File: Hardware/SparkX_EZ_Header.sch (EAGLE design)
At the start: 29 parts, among them J1 QWIIC_RIGHT_ANGLE

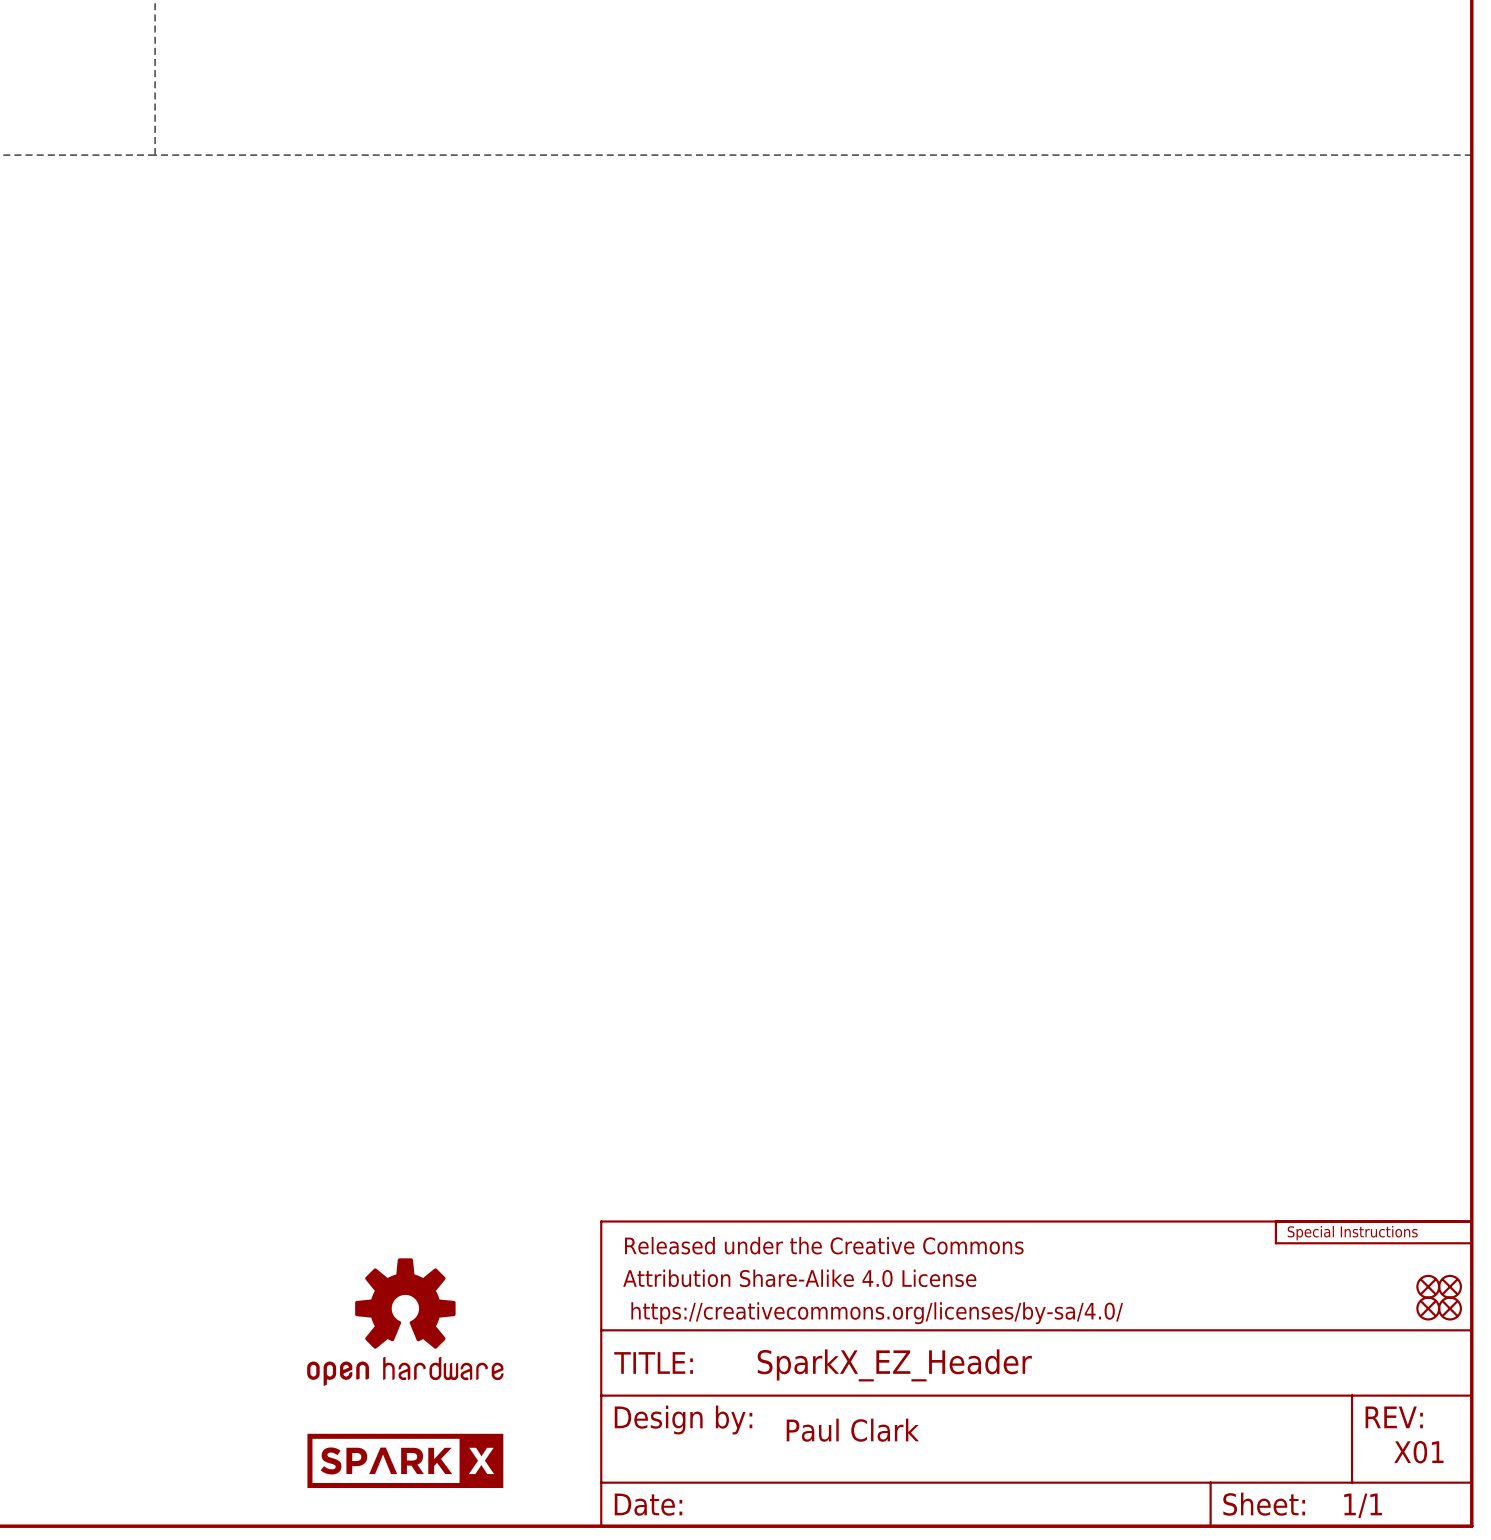
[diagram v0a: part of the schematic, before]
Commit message: Add bottom silk
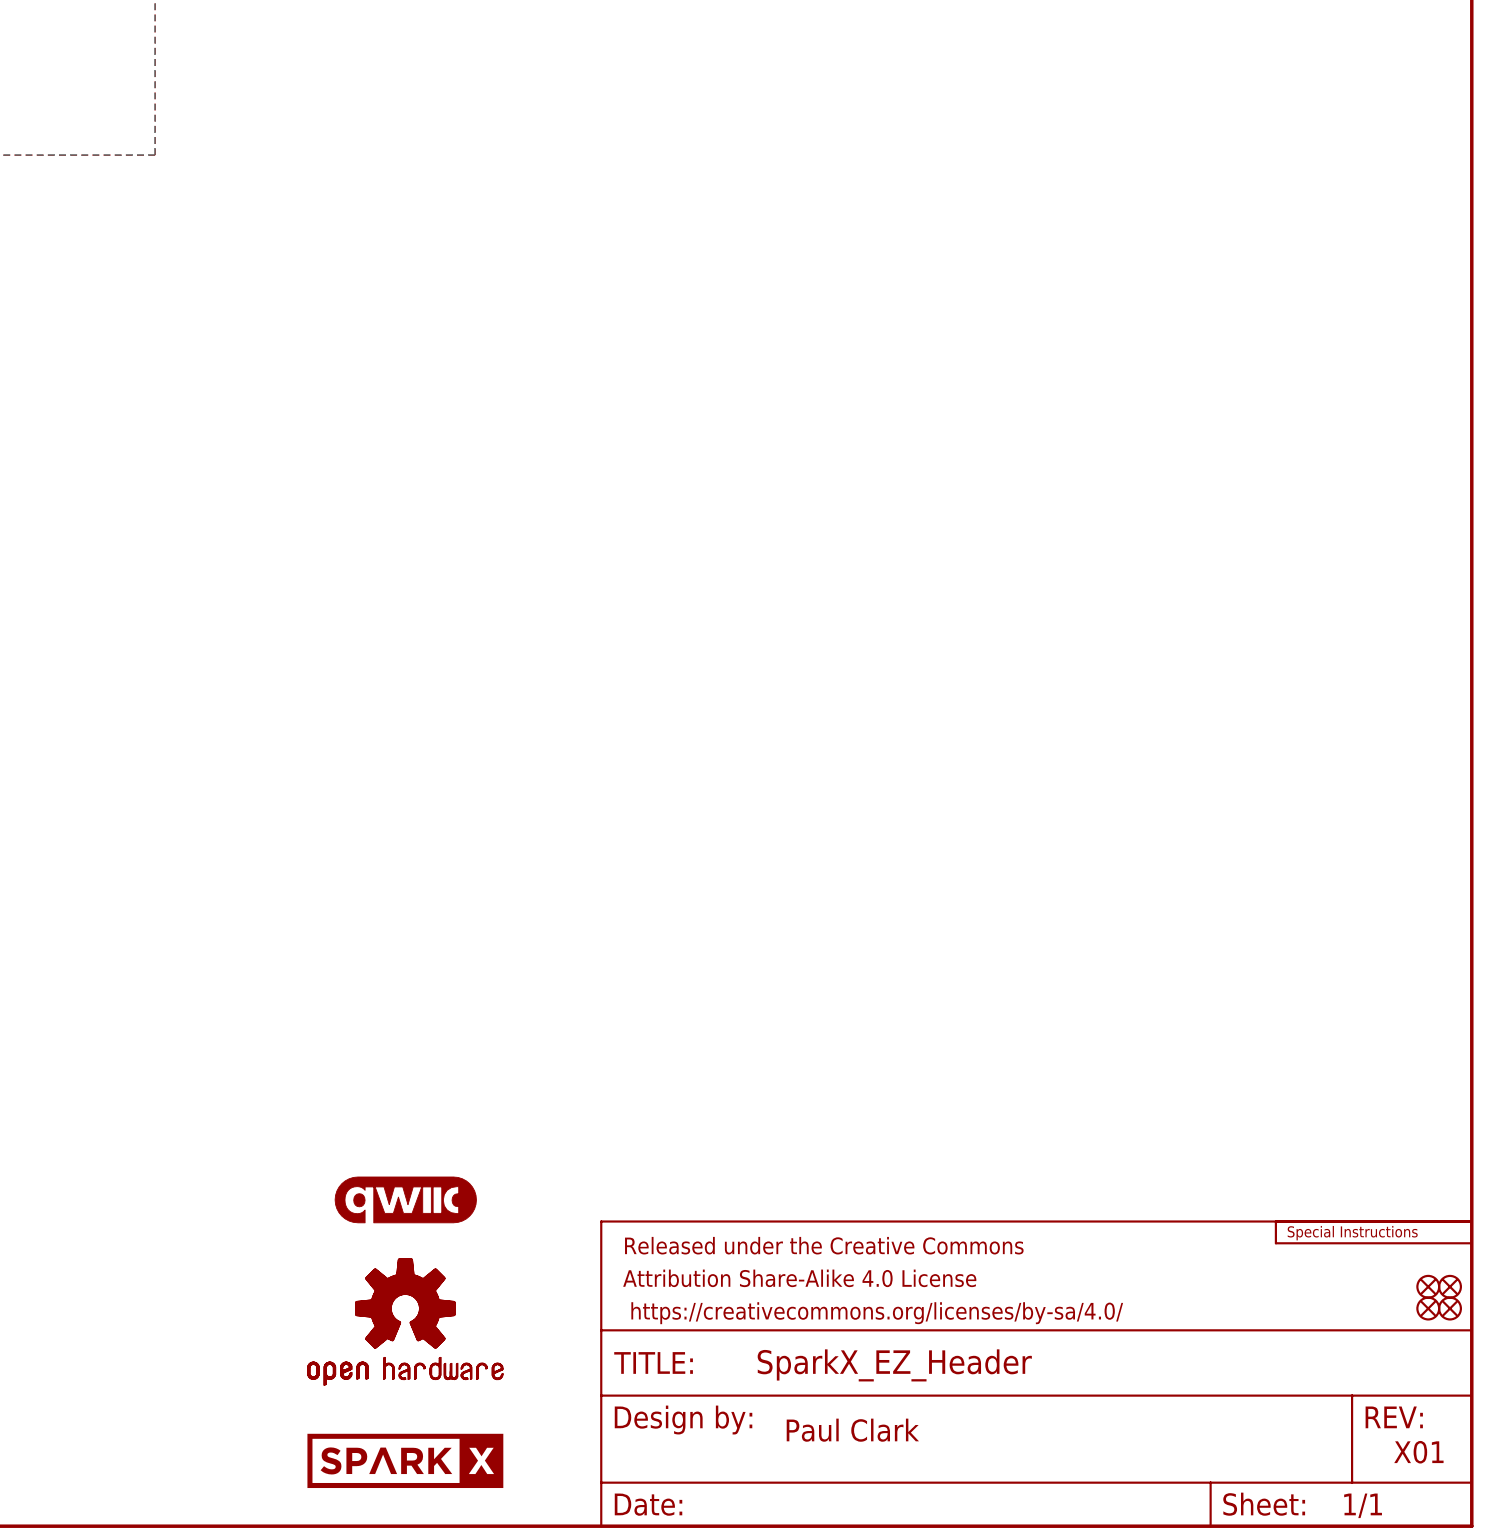
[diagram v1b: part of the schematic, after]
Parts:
- added LOGO3: OSHW-LOGOMINI, SparkFun-Aesthetics:OSHW-LOGOMINI
- added LOGO4: QWIIC_LOGO_5MM, SparkFun-Aesthetics:QWIIC_LOGO_5MM
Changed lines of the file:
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@@
 <part name="I2C" library="SparkFun-Jumpers" deviceset="JUMPER-SMT_3_2-NC_TRACE" device="_SILK" package3d_urn="urn:adsk.eagle:package:39289/1"/>
 <part name="SUPPLY5" library="SparkFun-PowerSymbols" deviceset="3.3V" device=""/>
+<part name="LOGO3" library="SparkFun-Aesthetics" deviceset="OSHW-LOGO" device="MINI"/>
+<part name="LOGO4" library="SparkFun-Aesthetics" deviceset="QWIIC_LOGO" device="_5MM"/>
 </parts>
 <sheets>
@@
 <text x="422.656" y="7.366" size="2.54" layer="94">X01</text>
 <wire x1="88.9" y1="160.02" x2="88.9" y2="279.4" width="0.2032" layer="97" style="longdash"/>
-<wire x1="431.8" y1="160.02" x2="278.13" y2="160.02" width="0.2032" layer="97" style="longdash"/>
 <wire x1="278.13" y1="160.02" x2="88.9" y2="160.02" width="0.2032" layer="97" style="longdash"/>
 <wire x1="201.93" y1="160.02" x2="201.93" y2="279.4" width="0.2032" layer="97" style="longdash"/>
@@
 <attribute name="VALUE" x="238.76" y="204.724" size="1.778" layer="96" align="bottom-center"/>
 </instance>
+<instance part="LOGO3" gate="G$1" x="307.34" y="25.4" smashed="yes"/>
+<instance part="LOGO4" gate="G$1" x="307.34" y="38.1" smashed="yes"/>
 </instances>
 <busses>

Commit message: Update 16-way FPC Connector
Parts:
- OUT: value FPC_16_0.5MM_BACKFLIP -> (none); device New_Parts_Connectors:FPC_16_0.5MM_BACKFLIP -> SparkFun-Connectors:CONN_16FPC_16_0.5MM
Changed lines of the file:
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@@
 <part name="FD3" library="SparkFun-Aesthetics" deviceset="FIDUCIAL" device="UFIDUCIAL" value="FIDUCIALUFIDUCIAL"/>
 <part name="FD4" library="SparkFun-Aesthetics" deviceset="FIDUCIAL" device="UFIDUCIAL" value="FIDUCIALUFIDUCIAL"/>
-<part name="OUT" library="New_Parts_Connectors" deviceset="FPC_16_0.5MM" device="_BACKFLIP"/>
+<part name="OUT" library="SparkFun-Connectors" deviceset="CONN_16" device="FPC_16_0.5MM"/>
 <part name="SUPPLY22" library="SparkFun-PowerSymbols" deviceset="3.3V" device=""/>
 <part name="SUPPLY27" library="SparkFun-PowerSymbols" deviceset="V_USB" device=""/>
@@
 <instance part="FD4" gate="G$1" x="429.26" y="27.94" smashed="yes"/>
 <instance part="LOGO2" gate="G$1" x="307.34" y="25.4" smashed="yes"/>
-<instance part="OUT" gate="G$1" x="53.34" y="215.9" smashed="yes" rot="MR0">
-<attribute name="NAME" x="55.88" y="236.474" size="1.778" layer="95" rot="MR0"/>
-<attribute name="VALUE" x="55.88" y="190.5" size="1.778" layer="96" rot="MR0"/>
+<instance part="OUT" gate="G$1" x="55.88" y="213.36" smashed="yes" rot="R180">
+<attribute name="NAME" x="53.34" y="192.786" size="1.778" layer="95" rot="R180"/>
+<attribute name="VALUE" x="58.42" y="238.76" size="1.778" layer="96" rot="R180"/>
 </instance>
 <instance part="SUPPLY22" gate="G$1" x="43.18" y="236.22" smashed="yes">
 <attribute name="VALUE" x="43.18" y="239.014" size="1.778" layer="96" align="bottom-center"/>
 </instance>
-<instance part="SUPPLY27" gate="G$1" x="35.56" y="195.58" smashed="yes">
-<attribute name="VALUE" x="35.56" y="198.374" size="1.778" layer="96" align="bottom-center"/>
+<instance part="SUPPLY27" gate="G$1" x="27.94" y="198.12" smashed="yes">
+<attribute name="VALUE" x="27.94" y="200.914" size="1.778" layer="96" align="bottom-center"/>
 </instance>
 <instance part="GND56" gate="1" x="40.64" y="187.96" smashed="yes">
@@
 <segment>
 <pinref part="SUPPLY22" gate="G$1" pin="3.3V"/>
-<wire x1="43.18" y1="236.22" x2="43.18" y2="231.14" width="0.1524" layer="91"/>
 <pinref part="OUT" gate="G$1" pin="2"/>
-<wire x1="43.18" y1="231.14" x2="45.72" y2="231.14" width="0.1524" layer="91"/>
 <pinref part="OUT" gate="G$1" pin="15"/>
+<wire x1="45.72" y1="231.14" x2="43.18" y2="231.14" width="0.1524" layer="91"/>
+<wire x1="43.18" y1="231.14" x2="43.18" y2="236.22" width="0.1524" layer="91"/>
 <wire x1="45.72" y1="198.12" x2="43.18" y2="198.12" width="0.1524" layer="91"/>
 <wire x1="43.18" y1="198.12" x2="43.18" y2="231.14" width="0.1524" layer="91"/>
@@
 <segment>
 <pinref part="OUT" gate="G$1" pin="16"/>
-<wire x1="45.72" y1="195.58" x2="43.18" y2="195.58" width="0.1524" layer="91"/>
-<wire x1="43.18" y1="195.58" x2="43.18" y2="193.04" width="0.1524" layer="91"/>
-<wire x1="43.18" y1="193.04" x2="35.56" y2="193.04" width="0.1524" layer="91"/>
+<wire x1="45.72" y1="195.58" x2="27.94" y2="195.58" width="0.1524" layer="91"/>
 <pinref part="SUPPLY27" gate="G$1" pin="V_USB"/>
-<wire x1="35.56" y1="193.04" x2="35.56" y2="195.58" width="0.1524" layer="91"/>
-</segment>
-<segment>
+<wire x1="27.94" y1="195.58" x2="27.94" y2="198.12" width="0.1524" layer="91"/>
+</segment>
+<segment>
